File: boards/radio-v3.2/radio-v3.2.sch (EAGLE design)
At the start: 32 parts, among them J1 HFW8R-1ST, J2 TC2050-IDC-NL, U1 ISM43340, U2 MPM3620GQV-P, U6 TPD2E2U06DRLR, U7 TPD2E2U06DRLR, U8 TPD2E2U06DRLR

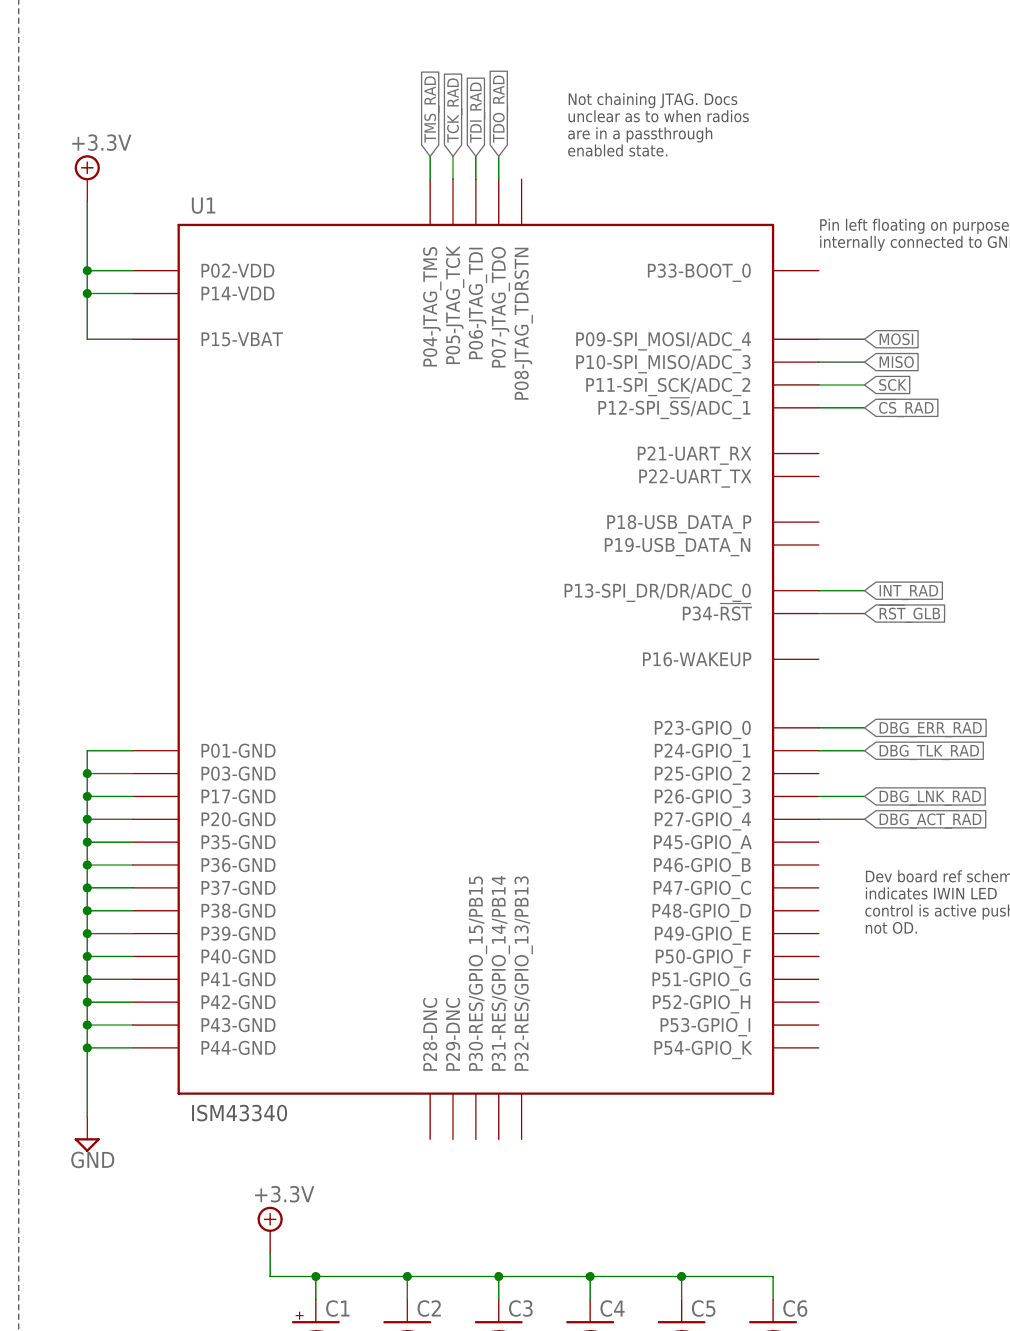
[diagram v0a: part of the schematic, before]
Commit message: radio done, kicker in progress
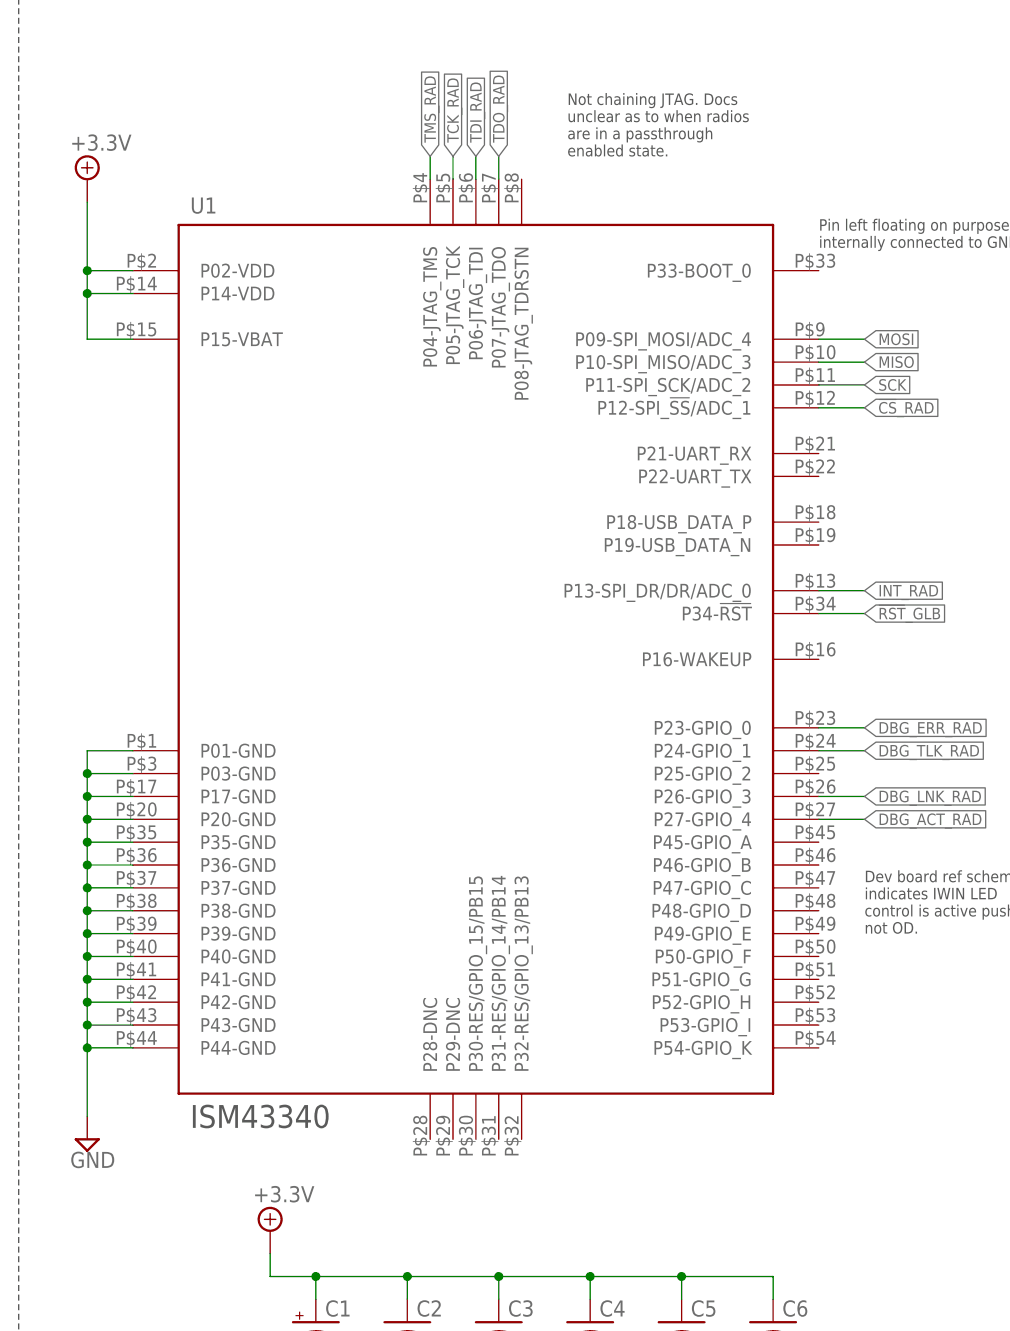
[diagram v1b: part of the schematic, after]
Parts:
- R1, R10, R2, R5, R6, R7, R8, R9: device resistor:R-US_R0603 -> rcl:R-US_R0603
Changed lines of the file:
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@@
 <?xml version="1.0" encoding="utf-8"?>
 <!DOCTYPE eagle SYSTEM "eagle.dtd">
-<eagle version="9.4.2">
+<eagle version="9.6.1">
 <drawing>
 <settings>
@@
 </classes>
 <parts>
-<part name="U2" library="mchair" deviceset="MPM3620GQV-P" device=""/>
+<part name="U2" library="mchair" deviceset="MPM3620GQV-P" device="" package3d_urn="urn:adsk.eagle:package:20143621/2"/>
 <part name="SUPPLY7" library="RoboJackets-Supplies" deviceset="+5.0V" device=""/>
-<part name="R2" library="resistor" library_urn="urn:adsk.eagle:library:348" deviceset="R-US_" device="R0603" package3d_urn="urn:adsk.eagle:package:23555/2" value="100k"/>
-<part name="R1" library="resistor" library_urn="urn:adsk.eagle:library:348" deviceset="R-US_" device="R0603" package3d_urn="urn:adsk.eagle:package:23555/2" value="88.7k 1%"/>
+<part name="R2" library="rcl" library_urn="urn:adsk.eagle:library:334" deviceset="R-US_" device="R0603" package3d_urn="urn:adsk.eagle:package:23555/3" value="100k"/>
+<part name="R1" library="rcl" library_urn="urn:adsk.eagle:library:334" deviceset="R-US_" device="R0603" package3d_urn="urn:adsk.eagle:package:23555/3" value="88.7k 1%"/>
 <part name="SUPPLY8" library="supply2" library_urn="urn:adsk.eagle:library:372" deviceset="GND" device=""/>
 <part name="C7" library="rcl" library_urn="urn:adsk.eagle:library:334" deviceset="C-US" device="C1210" package3d_urn="urn:adsk.eagle:package:23619/2" value="10uF 16V"/>
@@
 <part name="SUPPLY15" library="supply2" library_urn="urn:adsk.eagle:library:372" deviceset="GND" device=""/>
 <part name="SUPPLY14" library="RoboJackets-Supplies" deviceset="+3.3V" device=""/>
-<part name="D1" library="RoboJackets-LEDs" deviceset="LED-SMD" device="" technology="-GREEN" value="GREEN"/>
-<part name="D2" library="RoboJackets-LEDs" deviceset="LED-SMD" device="" technology="-GREEN" value="GREEN"/>
-<part name="R5" library="resistor" library_urn="urn:adsk.eagle:library:348" deviceset="R-US_" device="R0603" package3d_urn="urn:adsk.eagle:package:23555/2" value="1k"/>
-<part name="R6" library="resistor" library_urn="urn:adsk.eagle:library:348" deviceset="R-US_" device="R0603" package3d_urn="urn:adsk.eagle:package:23555/2" value="680"/>
+<part name="D1" library="RoboJackets-LEDs" deviceset="LED-SMD" device="" package3d_urn="urn:adsk.eagle:package:20143364/2" technology="-GREEN" value="GREEN"/>
+<part name="D2" library="RoboJackets-LEDs" deviceset="LED-SMD" device="" package3d_urn="urn:adsk.eagle:package:20143364/2" technology="-GREEN" value="GREEN"/>
+<part name="R5" library="rcl" library_urn="urn:adsk.eagle:library:334" deviceset="R-US_" device="R0603" package3d_urn="urn:adsk.eagle:package:23555/3" value="1k"/>
+<part name="R6" library="rcl" library_urn="urn:adsk.eagle:library:334" deviceset="R-US_" device="R0603" package3d_urn="urn:adsk.eagle:package:23555/3" value="680"/>
 <part name="SUPPLY16" library="supply2" library_urn="urn:adsk.eagle:library:372" deviceset="GND" device=""/>
 <part name="SUPPLY18" library="RoboJackets-Supplies" deviceset="+3.3V" device=""/>
@@
 <part name="SUPPLY1" library="RoboJackets-Supplies" deviceset="+3.3V" device=""/>
 <part name="SUPPLY2" library="supply2" library_urn="urn:adsk.eagle:library:372" deviceset="GND" device=""/>
-<part name="U1" library="RoboJackets-RF" deviceset="ISM43340" device=""/>
-<part name="C1" library="RoboJackets-Capacitors" deviceset="ECA-0JM221" device="" value="220uF"/>
+<part name="U1" library="RoboJackets-RF" deviceset="ISM43340" device="" package3d_urn="urn:adsk.eagle:package:20308189/2"/>
+<part name="C1" library="RoboJackets-Capacitors" deviceset="ECA-0JM221" device="" package3d_urn="urn:adsk.eagle:package:20308170/2" value="220uF"/>
 <part name="C4" library="rcl" library_urn="urn:adsk.eagle:library:334" deviceset="C-US" device="C0603" package3d_urn="urn:adsk.eagle:package:23616/2" value="1uF"/>
 <part name="C5" library="rcl" library_urn="urn:adsk.eagle:library:334" deviceset="C-US" device="C0603" package3d_urn="urn:adsk.eagle:package:23616/2" value="0.1uF"/>
@@
 <part name="SUPPLY4" library="supply2" library_urn="urn:adsk.eagle:library:372" deviceset="GND" device=""/>
 <part name="SUPPLY3" library="RoboJackets-Supplies" deviceset="+3.3V" device=""/>
-<part name="D4" library="RoboJackets-LEDs" deviceset="LED-SMD" device="" technology="-GREEN" value="GREEN"/>
-<part name="D3" library="RoboJackets-LEDs" deviceset="LED-SMD" device="" technology="-RED" value="RED"/>
+<part name="D4" library="RoboJackets-LEDs" deviceset="LED-SMD" device="" package3d_urn="urn:adsk.eagle:package:20143364/2" technology="-GREEN" value="GREEN"/>
+<part name="D3" library="RoboJackets-LEDs" deviceset="LED-SMD" device="" package3d_urn="urn:adsk.eagle:package:20143364/2" technology="-RED" value="RED"/>
 <part name="SUPPLY25" library="supply2" library_urn="urn:adsk.eagle:library:372" deviceset="GND" device=""/>
-<part name="J2" library="RoboJackets-Connectors" deviceset="TC2050-IDC-NL" device=""/>
+<part name="J2" library="RoboJackets-Connectors" deviceset="TC2050-IDC-NL" device="" package3d_urn="urn:adsk.eagle:package:20308059/2"/>
 <part name="SUPPLY19" library="RoboJackets-Supplies" deviceset="+3.3V" device=""/>
 <part name="SUPPLY20" library="supply2" library_urn="urn:adsk.eagle:library:372" deviceset="GND" device=""/>
-<part name="R8" library="resistor" library_urn="urn:adsk.eagle:library:348" deviceset="R-US_" device="R0603" package3d_urn="urn:adsk.eagle:package:23555/2" value="1k"/>
-<part name="R7" library="resistor" library_urn="urn:adsk.eagle:library:348" deviceset="R-US_" device="R0603" package3d_urn="urn:adsk.eagle:package:23555/2" value="1k"/>
-<part name="R9" library="resistor" library_urn="urn:adsk.eagle:library:348" deviceset="R-US_" device="R0603" package3d_urn="urn:adsk.eagle:package:23555/2" value="1k"/>
-<part name="R10" library="resistor" library_urn="urn:adsk.eagle:library:348" deviceset="R-US_" device="R0603" package3d_urn="urn:adsk.eagle:package:23555/2" value="1k"/>
-<part name="D5" library="RoboJackets-LEDs" deviceset="LED-SMD" device="" technology="-GREEN" value="GREEN"/>
-<part name="D6" library="RoboJackets-LEDs" deviceset="LED-SMD" device="" technology="-YELLOW" value="YELLOW"/>
+<part name="R8" library="rcl" library_urn="urn:adsk.eagle:library:334" deviceset="R-US_" device="R0603" package3d_urn="urn:adsk.eagle:package:23555/3" value="1k"/>
+<part name="R7" library="rcl" library_urn="urn:adsk.eagle:library:334" deviceset="R-US_" device="R0603" package3d_urn="urn:adsk.eagle:package:23555/3" value="1k"/>
+<part name="R9" library="rcl" library_urn="urn:adsk.eagle:library:334" deviceset="R-US_" device="R0603" package3d_urn="urn:adsk.eagle:package:23555/3" value="1k"/>
+<part name="R10" library="rcl" library_urn="urn:adsk.eagle:library:334" deviceset="R-US_" device="R0603" package3d_urn="urn:adsk.eagle:package:23555/3" value="1k"/>
+<part name="D5" library="RoboJackets-LEDs" deviceset="LED-SMD" device="" package3d_urn="urn:adsk.eagle:package:20143364/2" technology="-GREEN" value="GREEN"/>
+<part name="D6" library="RoboJackets-LEDs" deviceset="LED-SMD" device="" package3d_urn="urn:adsk.eagle:package:20143364/2" technology="-YELLOW" value="YELLOW"/>
 <part name="FRAME1" library="RoboJackets-Frames" deviceset="FRAME_B_L" device="">
 <attribute name="SCH_DESC" value="Dual TX/RX radio module using ISM43340"/>
@@
 <part name="SUPPLY9" library="RoboJackets-Supplies" deviceset="+5.0V" device=""/>
 <part name="SUPPLY10" library="supply2" library_urn="urn:adsk.eagle:library:372" deviceset="GND" device=""/>
-<part name="J1" library="RoboJackets-Connectors" deviceset="HFW8" device="R-1ST"/>
+<part name="J1" library="RoboJackets-Connectors" deviceset="HFW8" device="R-1ST" package3d_urn="urn:adsk.eagle:package:20000151/2"/>
 <part name="SUPPLY11" library="supply2" library_urn="urn:adsk.eagle:library:372" deviceset="GND" device=""/>
 <part name="SUPPLY12" library="supply2" library_urn="urn:adsk.eagle:library:372" deviceset="GND" device=""/>
 <part name="SUPPLY29" library="supply2" library_urn="urn:adsk.eagle:library:372" deviceset="GND" device=""/>
-<part name="U6" library="radio_in_progress" deviceset="TPD2E2U06DRLR" device=""/>
-<part name="U7" library="radio_in_progress" deviceset="TPD2E2U06DRLR" device=""/>
-<part name="U8" library="radio_in_progress" deviceset="TPD2E2U06DRLR" device=""/>
+<part name="U6" library="radio_in_progress" deviceset="TPD2E2U06DRLR" device="" package3d_urn="urn:adsk.eagle:package:20308181/2"/>
+<part name="U7" library="radio_in_progress" deviceset="TPD2E2U06DRLR" device="" package3d_urn="urn:adsk.eagle:package:20308181/2"/>
+<part name="U8" library="radio_in_progress" deviceset="TPD2E2U06DRLR" device="" package3d_urn="urn:adsk.eagle:package:20308181/2"/>
 <part name="C2" library="rcl" library_urn="urn:adsk.eagle:library:334" deviceset="C-US" device="C0805" package3d_urn="urn:adsk.eagle:package:23617/2" value="10uF"/>
 <part name="C3" library="rcl" library_urn="urn:adsk.eagle:library:334" deviceset="C-US" device="C0805" package3d_urn="urn:adsk.eagle:package:23617/2" value="10uF"/>
